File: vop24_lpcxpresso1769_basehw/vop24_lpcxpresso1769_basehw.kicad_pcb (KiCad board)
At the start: 2 copper layers, 113 parts, among them J1 Micro_SD_Card, J101 Conn_01x03_Male, J201 Screw_Terminal_01x02, J301 USB_B_Micro, J302 Conn_01x06_Male, J303 Conn_01x05_Male, J304 Screw_Terminal_01x02, J401 Conn_01x02, J402 Conn_01x02, J403 Conn_01x02, J404 Conn_01x04, J405 Conn_01x04, J406 Conn_01x04, U1 LPCXpresso1769, U101 MCP1700T-3302E_TT, U102 MCP1700T-3302E_TT, U103 TPS63001, U201 LM358, U301 TPD4S014, U302 LTC4411, U303 LT1512, U401 ADS1292, U402 LM334, U403 LM334, U404 LM334

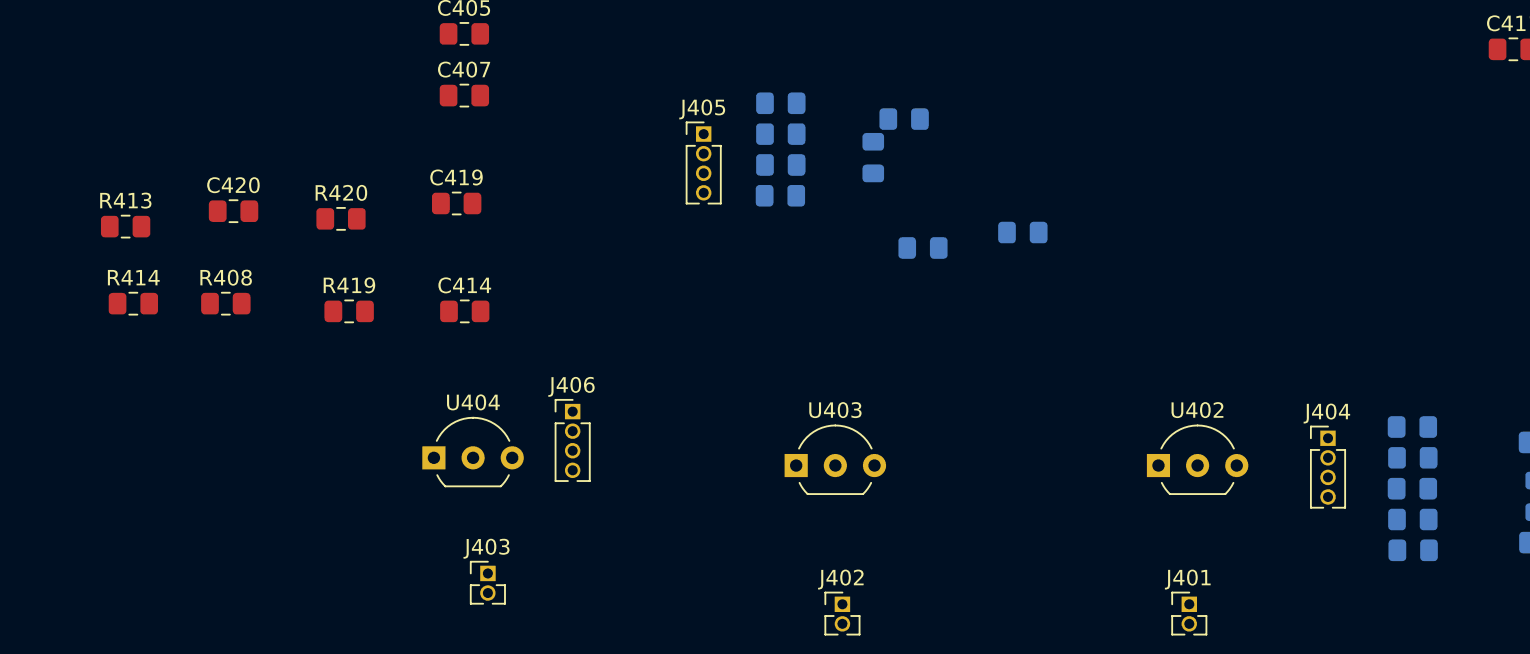
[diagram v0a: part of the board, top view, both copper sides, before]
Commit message: Cambios menores en circuito ADS
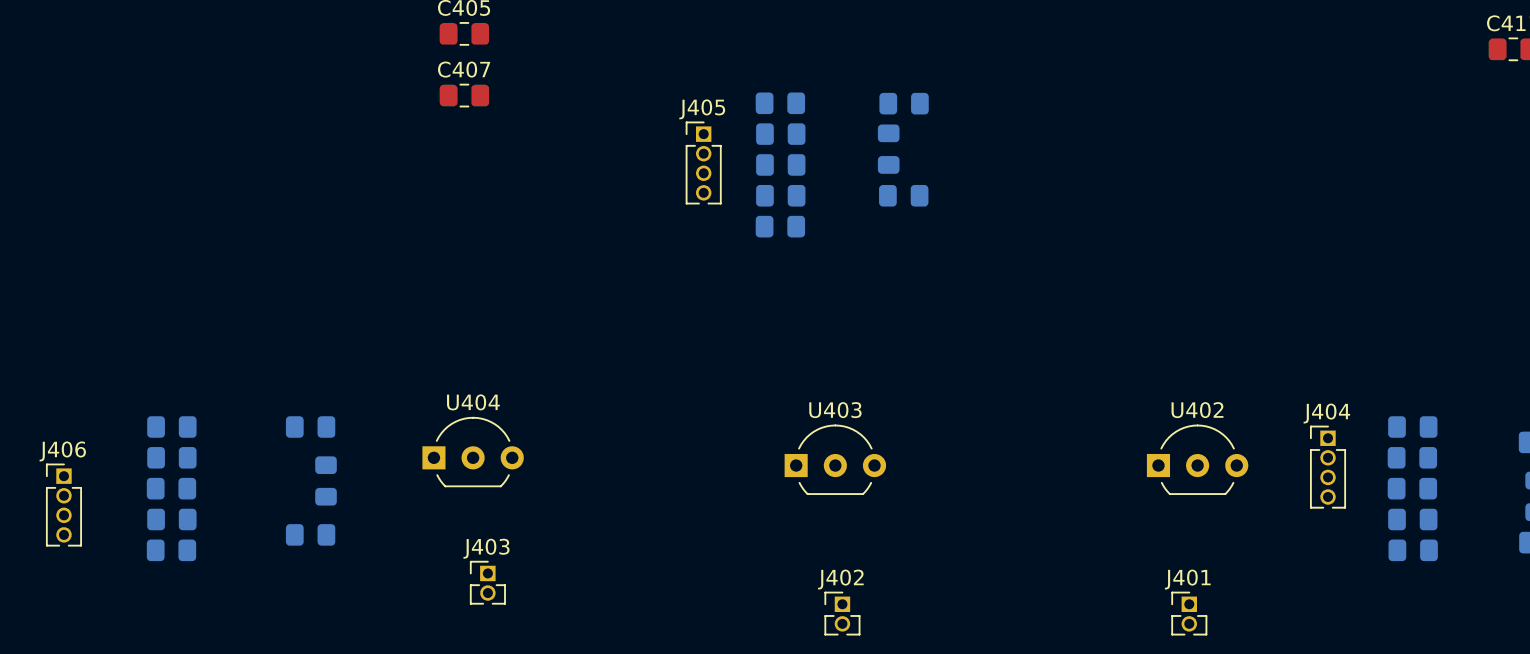
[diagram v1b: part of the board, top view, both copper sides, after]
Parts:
- C414, C419, C420, R408, R413, R414, R419, R420: moved to B.Cu
- moved J406 33.3 mm to (30.5, 68.2)
- moved C419 23.5 mm to (46.5, 72.0), turned to 180 degrees
- moved R417 17.8 mm to (77.0, 44.0)
- moved R419 17.7 mm to (37.5, 71.0), turned to 180 degrees
- moved R420 17.4 mm to (37.5, 65.0), turned to 180 degrees
- moved R413 17.3 mm to (37.5, 69.0), turned to 180 degrees
- moved R408 16.4 mm to (37.5, 73.0)
- moved C420 14.9 mm to (46.5, 65.0), turned to 180 degrees
- moved C414 14.2 mm to (47.5, 68.5), turned to 90 degrees
- moved R414 10.3 mm to (37.5, 67.0), turned to 180 degrees
- moved R412 4.00 mm to (77.0, 48.0)
- moved R418 4.00 mm to (77.0, 50.0)
- moved C417 3.61 mm to (85.0, 50.0)
- moved R407 2.00 mm to (77.0, 52.0)
- moved R410 2.00 mm to (118.0, 67.0)
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
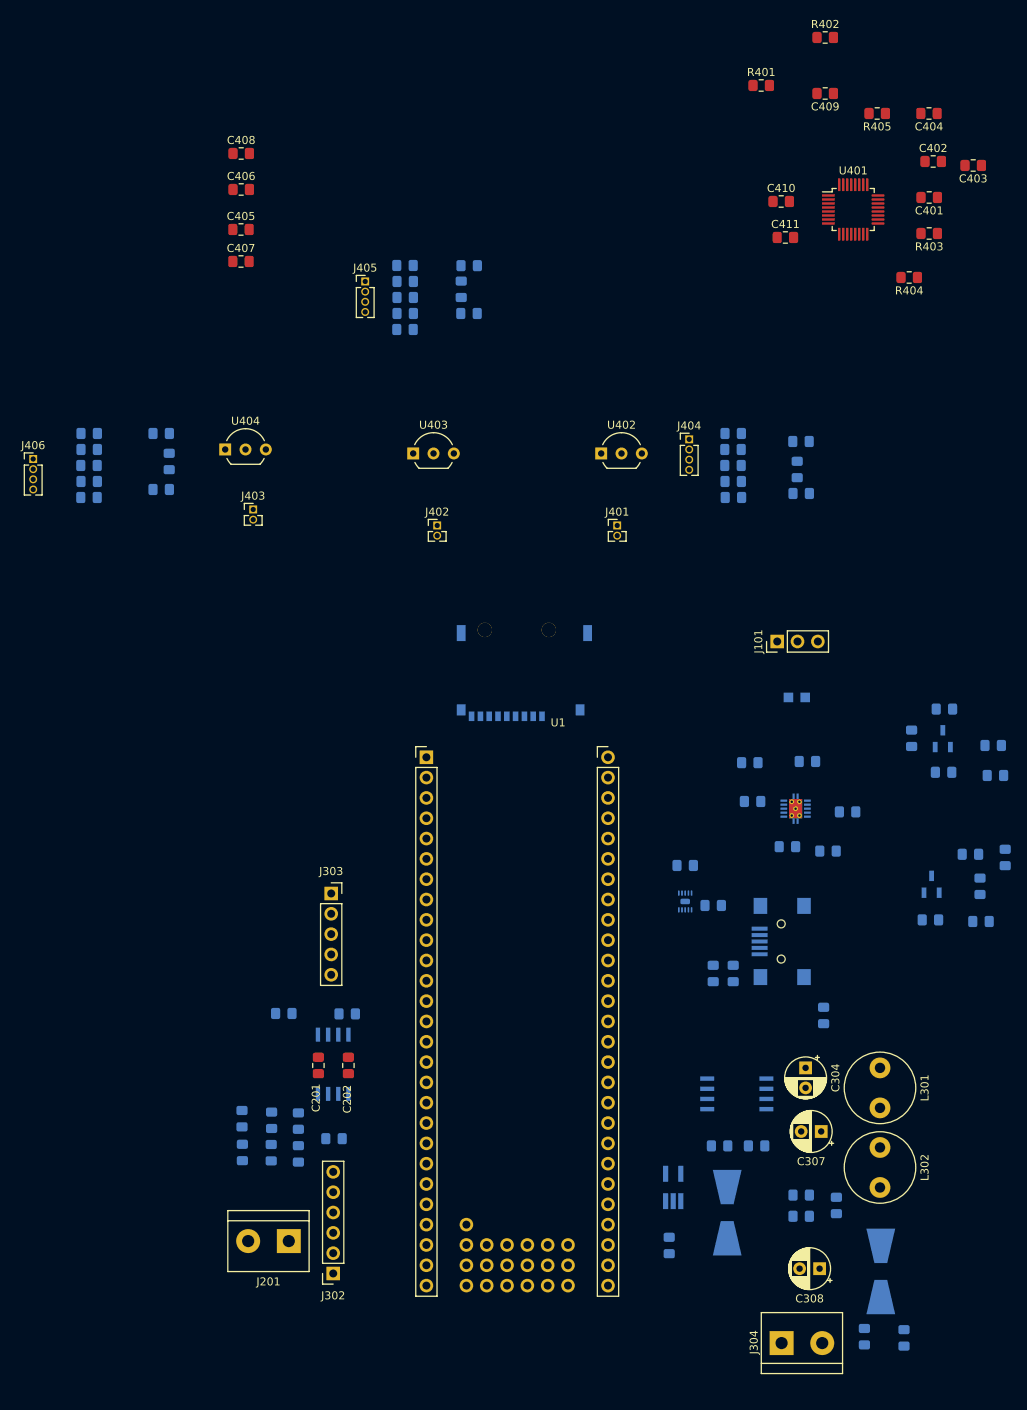
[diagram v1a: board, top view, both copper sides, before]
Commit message: PCB: posicionamiento preruteo. ESQ: cambio de footprint de conectores
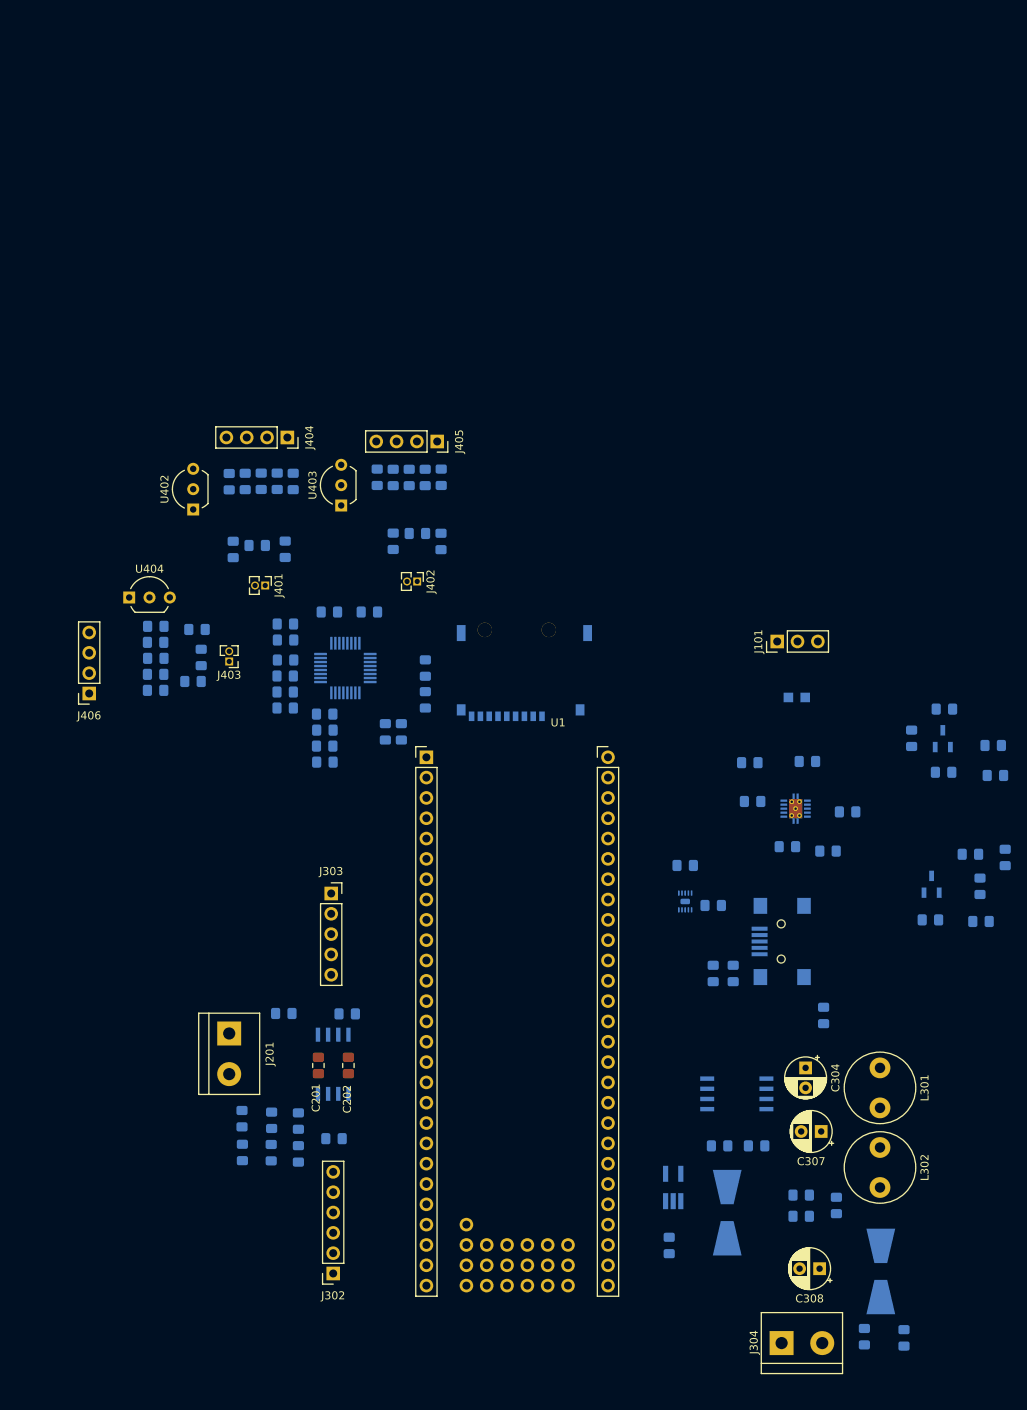
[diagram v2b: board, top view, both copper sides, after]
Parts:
- C401, C402, C403, C404, C405, C406, C407, C408, C409, C410, C411, R401, R402, R403, R404, R405, U401: moved to B.Cu
- J404, J405, J406: footprint Connector_PinHeader_1.27mm:PinHeader_1x04_P1.27mm_Vertical -> Connector_PinSocket_2.54mm:PinSocket_1x04_P2.54mm_Vertical
- moved R405 103.5 mm to (62.0, 97.3), turned to 0 degrees
- moved C402 103.4 mm to (62.0, 95.3), turned to 180 degrees
- moved C404 102.9 mm to (74.5, 102.3), turned to 90 degrees
- moved C403 100.6 mm to (76.5, 102.3), turned to 90 degrees
- moved R403 100.0 mm to (62.0, 99.3), turned to 0 degrees
- moved R402 99.6 mm to (62.0, 88.8), turned to 180 degrees
- moved C409 96.0 mm to (62.0, 90.8), turned to 0 degrees
- moved R401 93.2 mm to (62.0, 93.3), turned to 180 degrees
- moved C401 86.2 mm to (79.5, 94.3), turned to 270 degrees
- moved U401 85.5 mm to (69.5, 94.3), turned to 270 degrees
- moved R404 80.3 mm to (79.5, 98.3), turned to 90 degrees
- moved C410 76.3 mm to (67.5, 87.3)
- moved C415 71.3 mm to (55.5, 79.5), turned to 90 degrees
- moved C408 70.9 mm to (66.9, 100.1), turned to 180 degrees
- moved C406 70.4 mm to (66.9, 104.1), turned to 180 degrees
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
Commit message: PCB: ruteo e ubicacion de USB.    ESQ: cambios de etiquetas de gnd en usb
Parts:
- C201, C202, C304, C307, L301, L302: moved to B.Cu
- moved C102 47.0 mm to (111.1, 66.3)
- moved C106 47.0 mm to (115.1, 70.5)
- moved C107 47.0 mm to (103.1, 75.5)
- moved U102 47.0 mm to (113.6, 84.5)
- moved C103 47.0 mm to (90.9, 69.3)
- moved C104 47.0 mm to (95.6, 79.8)
- moved R102 47.0 mm to (115.2, 62.6)
- moved U103 47.0 mm to (96.6, 75.1)
- moved U101 47.0 mm to (115.0, 66.3)
- moved C101 47.0 mm to (122.8, 81.2)
- moved C105 47.0 mm to (113.5, 89.0)
- moved D101 47.0 mm to (118.5, 80.8)
- moved D102 47.0 mm to (121.6, 71.0)
- moved FB101 47.0 mm to (96.8, 61.2)
- moved J101 47.0 mm to (94.3, 54.2)
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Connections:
- C302 pad 2: /Comunicacion/DGND -> /Comunicacion/USB_GND
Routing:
- net /VUSB_OUT: track 0.00 -> 55.4 mm
- net /USB_ID: track 0.00 -> 49.6 mm
- net /TPD_~ACK: track 0.00 -> 41.6 mm, vias 0 -> 2
- net Net-(L302-Pad2): track 0.00 -> 41.3 mm
- net /TPD_~EN: track 0.00 -> 37.0 mm, vias 0 -> 2
- net /Comunicacion/USB_GND: track 0.00 -> 35.4 mm, vias 0 -> 2
- net /DGND: track 0.00 -> 34.8 mm
- net Net-(C307-Pad1): track 0.00 -> 28.2 mm
- net /USB_D+: track 0.00 -> 28.0 mm, vias 0 -> 2
- net Net-(C302-Pad1): track 0.00 -> 21.2 mm, vias 0 -> 2
- net /USB_D-: track 0.00 -> 21.1 mm
- net /analogico/VBAT: track 0.00 -> 15.5 mm
- net Net-(C307-Pad2): track 0.00 -> 11.8 mm
- net /fuentesLDO/VCC_NREG: track 0.00 -> 9.23 mm
- net /LTC4411_STAT: track 0.00 -> 7.70 mm
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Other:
- net class Default: clearance 0.2 -> 0.1; via_dia 0.8 -> 0.7; via_drill 0.4 -> 0.5
- net class mayer8mils added: clearance 0.1, trace_width 0.2, via_dia 0.8, via_drill 0.4
- rule trace_clearance: 0.2 -> 0.1
- rule trace_min: 0.2 -> 0.15
- rule via_min_drill: 0.3 -> 0.4
- rule via_min_size: 0.4 -> 0.7

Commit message: PCB: progreso en el ruteo
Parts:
- moved D102 27.4 mm to (115.0, 97.5), turned to 180 degrees
- moved C106 25.0 mm to (115.1, 95.5)
- moved R105 24.9 mm to (119.5, 92.0), turned to 0 degrees
- moved U101 24.5 mm to (115.0, 90.8)
- moved R102 24.2 mm to (119.5, 86.5)
- moved C102 24.2 mm to (119.5, 89.0), turned to 0 degrees
- moved D101 24.2 mm to (119.0, 105.0), turned to 0 degrees
- moved R104 22.2 mm to (119.0, 107.0), turned to 180 degrees
- moved C101 22.1 mm to (119.0, 103.0), turned to 0 degrees
- moved C105 20.0 mm to (114.0, 109.0)
- moved R101 19.8 mm to (119.0, 109.0)
- moved U102 19.5 mm to (113.6, 104.0)
- moved R303 5.94 mm to (123.5, 136.5), turned to 270 degrees
- moved C303 2.05 mm to (110.0, 164.4), turned to 270 degrees
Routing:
- net /DGND: track 34.8 -> 203.3 mm
- net Net-(R307-Pad1): track 5.93 -> 66.2 mm, vias 0 -> 2
- net /analogico/VBAT: track 15.5 -> 56.1 mm
- net /DVCC: track 0.00 -> 38.4 mm
- net /LT1512_SS: track 0.00 -> 32.2 mm
- net /VUSB_OUT: track 55.4 -> 87.4 mm, vias 0 -> 2
- net /fuentesLDO/VCC_NREG: track 9.23 -> 30.2 mm
- net /Comunicacion/USB_GND: track 35.4 -> 50.3 mm
- net /AGND: track 0.00 -> 14.6 mm
- net Net-(C306-Pad1): track 0.00 -> 9.55 mm
- net Net-(D102-Pad1): track 0.00 -> 9.01 mm
- net Net-(C305-Pad1): track 0.00 -> 8.53 mm
- net Net-(C307-Pad2): track 11.8 -> 18.2 mm
- net /AVCC: track 0.00 -> 5.65 mm
- net Net-(C305-Pad2): track 0.00 -> 2.58 mm
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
